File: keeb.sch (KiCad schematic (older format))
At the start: 134 parts, among them SW101 SW_Push, SW102 SW_Push, SW103 SW_Push, SW104 SW_Push, SW105 SW_Push, SW106 SW_Push, SW107 SW_Push, SW108 SW_Push, SW109 SW_Push, SW110 SW_Push, SW111 SW_Push, SW112 SW_Push, SW113 SW_Push, SW114 SW_Push, SW115 SW_Push, SW116 SW_Push, SW117 SW_Push, SW118 SW_Push, SW119 SW_Push, SW120 SW_Push, SW121 SW_Push, SW122 SW_Push, SW123 SW_Push, SW124 SW_Push, SW125 SW_Push, SW126 SW_Push, SW127 SW_Push, SW128 SW_Push, SW129 SW_Push, SW130 SW_Push, SW131 SW_Push, SW132 SW_Push, SW133 SW_Push, SW134 SW_Push, SW135 SW_Push, SW136 SW_Push, SW137 SW_Push, SW138 SW_Push, SW139 SW_Push, SW140 SW_Push, SW141 SW_Push, SW142 SW_Push, SW143 SW_Push, SW144 SW_Push, SW145 SW_Push, SW146 SW_Push, SW147 SW_Push, SW148 SW_Push, SW149 SW_Push, SW150 SW_Push, SW151 SW_Push, SW152 SW_Push, SW153 SW_Push, SW154 SW_Push, SW155 SW_Push, SW156 SW_Push, SW157 SW_Push, SW158 SW_Push, SW159 SW_Push, SW160 SW_Push, SW161 SW_Push, SW162 SW_Push, SW163 SW_Push, SW164 SW_Push, SW165 SW_Push, SW166 SW_Push

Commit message: schem compl, layout sw, mat  routing
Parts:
- added C101, C102, C103, C104, C105: 100n, Capacitor_SMD:C_0603_1608Metric_Pad1.08x0.95mm_HandSolder, symbol Device:C_Small
- added C106, C107: 20p, Capacitor_SMD:C_0603_1608Metric_Pad1.08x0.95mm_HandSolder, symbol Device:C_Small
- added C108: 1u, Capacitor_SMD:C_0603_1608Metric_Pad1.08x0.95mm_HandSolder, symbol Device:C_Small
- added F101: 500mA, Fuse:Fuse_1206_3216Metric_Pad1.42x1.75mm_HandSolder, symbol Device:Polyfuse_Small
- added J101: USB_C_Receptacle_USB2.0, Connector_USB:USB_C_Receptacle_Palconn_UTC16-G, symbol Connector:USB_C_Receptacle_USB2.0
- added R101, R102: 5K1, Resistor_SMD:R_0603_1608Metric_Pad0.98x0.95mm_HandSolder, symbol Device:R_Small
- added R103, R104: 22, Resistor_SMD:R_0603_1608Metric_Pad0.98x0.95mm_HandSolder, symbol Device:R_Small
- added R105, R106: 10k, Resistor_SMD:R_0603_1608Metric_Pad0.98x0.95mm_HandSolder, symbol Device:R_Small
- added SW167: SW_Push, Button_Switch_THT:SW_PUSH_6mm_H5mm, symbol Switch:SW_Push
- added U101: TPD2EUSB30, Package_TO_SOT_SMD:Texas_DRT-3, symbol Power_Protection:TPD2EUSB30
- added U102: ATmega32U4-AU, Package_QFP:TQFP-44_10x10mm_P0.8mm, symbol MCU_Microchip_ATmega:ATmega32U4-AU
- added Y101: 16MHZ/20PF, Crystal:Crystal_HC49-4H_Vertical, symbol Device:Crystal
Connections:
- net COL_0: now also U102.28 (PB4)
- net COL_1: now also U102.29 (PB5)
- net COL_10: now also U102.25 (PD4)
- net COL_11: now also U102.22 (PD5)
- net COL_12: now also U102.26 (PD6)
- net COL_13: now also U102.27 (PD7)
- net COL_2: now also U102.30 (PB6)
- net COL_3: now also U102.12 (PB7)
- net COL_4: now also U102.31 (PC6)
- net COL_5: now also U102.32 (PC7)
- net COL_6: now also U102.18 (PD0)
- net COL_7: now also U102.19 (PD1)
- net COL_8: now also U102.20 (PD2)
- net COL_9: now also U102.21 (PD3)
- net ROW_0: now also D113.1 (K), D114.1 (K), U102.41 (PF0)
- net ROW_1: now also U102.40 (PF1)
- net ROW_2: now also U102.39 (PF4)
- net ROW_3: now also U102.38 (PF5)
- net ROW_4: now also U102.37 (PF6)
- new net +5V: C101.1, C102.1, C103.1, C104.1, C105.1, F101.1, R105.2, U102.14 (VCC), U102.2 (UVCC), U102.24 (AVCC), U102.34 (VCC), U102.44 (AVCC), U102.7 (VBUS)
- new net CC1: J101.A5 (CC1), R101.1
- new net CC2: J101.B5 (CC2), R102.1
- new net D+: J101.A6 (D+), J101.B6 (D+), R103.2, U101.1 (D+)
- new net D-: J101.A7 (D-), J101.B7 (D-), R104.2, U101.2 (D-)
- new net GND: C101.2, C102.2, C103.2, C104.2, C105.2, C106.2, C107.2, C108.1, J101.A1 (GND), J101.A12 (GND), J101.B1 (GND), J101.B12 (GND), R101.2, R102.2, R106.1, SW167.2, U101.3 (GND), U102.15 (GND), U102.23 (GND), U102.35 (GND), U102.43 (GND), U102.5 (UGND)
- new net MISO: U102.11 (PB3)
- new net MOSI: U102.10 (PB2)
- new net SCLK: U102.9 (PB1)
- new net UCAP: C108.2, U102.6 (UCAP)
- new net USB+: R103.1, U102.4 (D+)
- new net USB-: R104.1, U102.3 (D-)
- new net VBUS: F101.2, J101.A4 (VBUS), J101.A9 (VBUS), J101.B4 (VBUS), J101.B9 (VBUS)
- new net XTAL1: C106.1, U102.17 (XTAL1), Y101.1
- new net XTAL2: C107.1, U102.16 (XTAL2), Y101.2
- new net ~HWB: R106.2, U102.33 (~HWB~/PE2)
- new net ~RESET: R105.1, SW167.1, U102.13 (~RESET)
- no-connect marks 0 -> 7
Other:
- moved on the sheet: D101, D102, D103, D104, D105, D106, D107, D108, D109, D110, D111, D112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

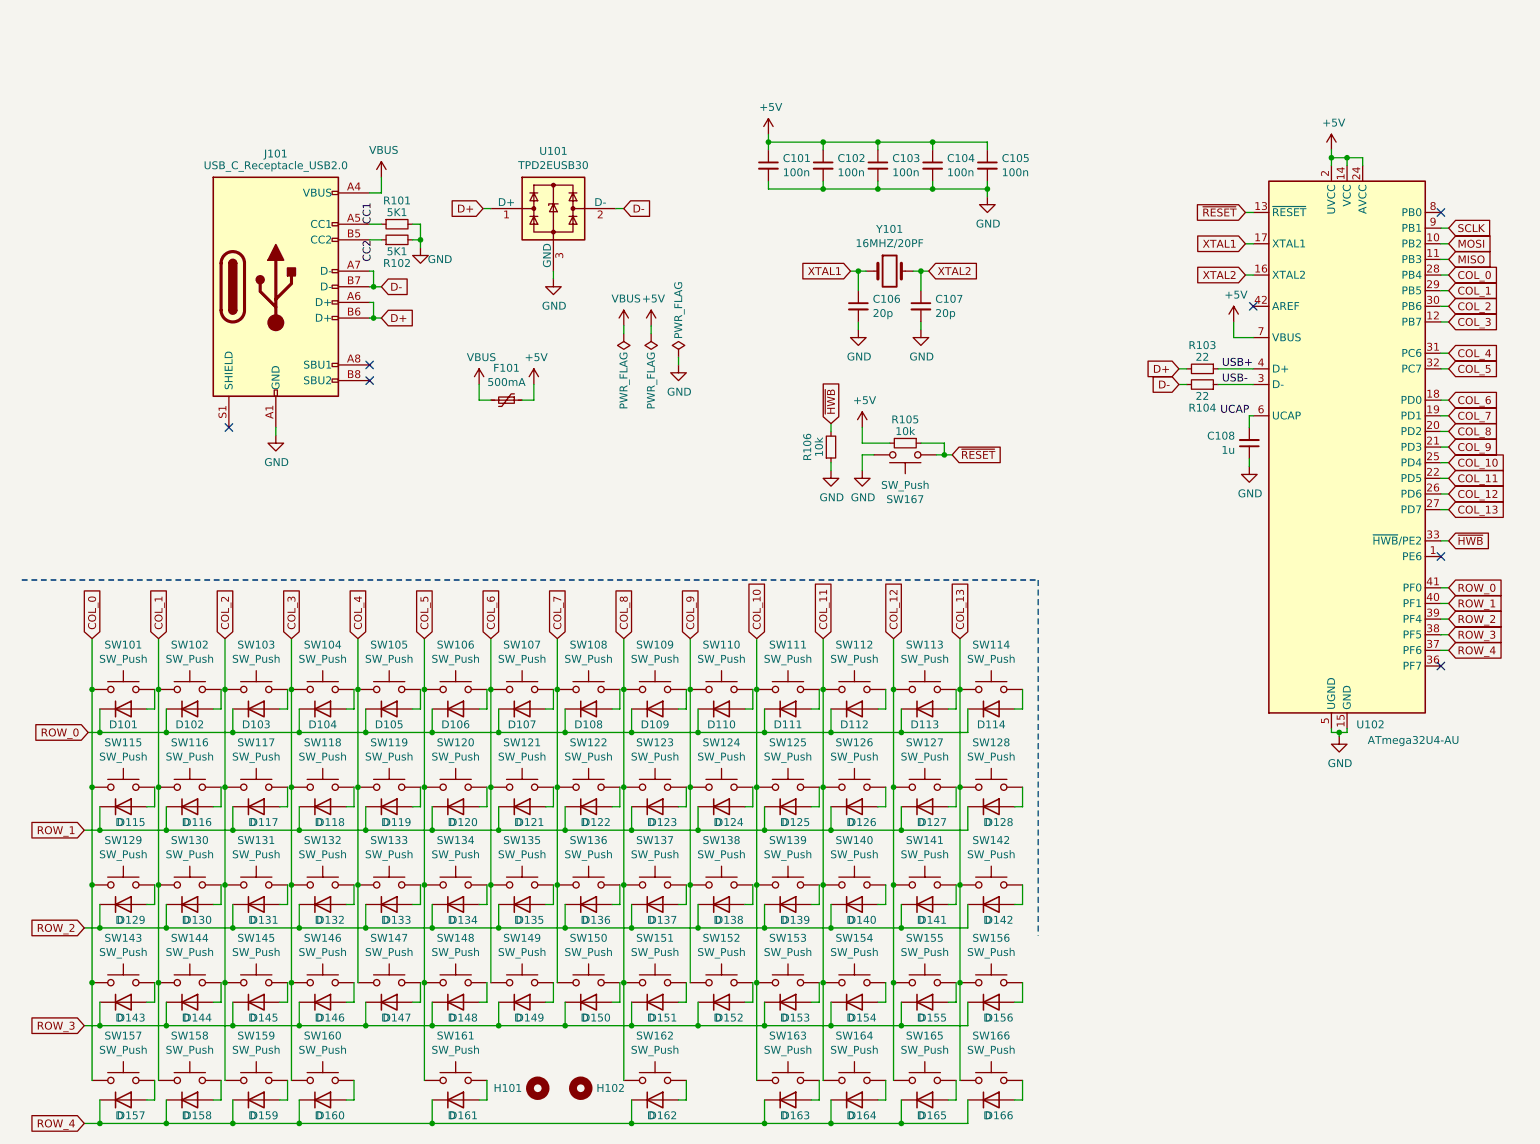
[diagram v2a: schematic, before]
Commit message: col, USB, and gnd layout
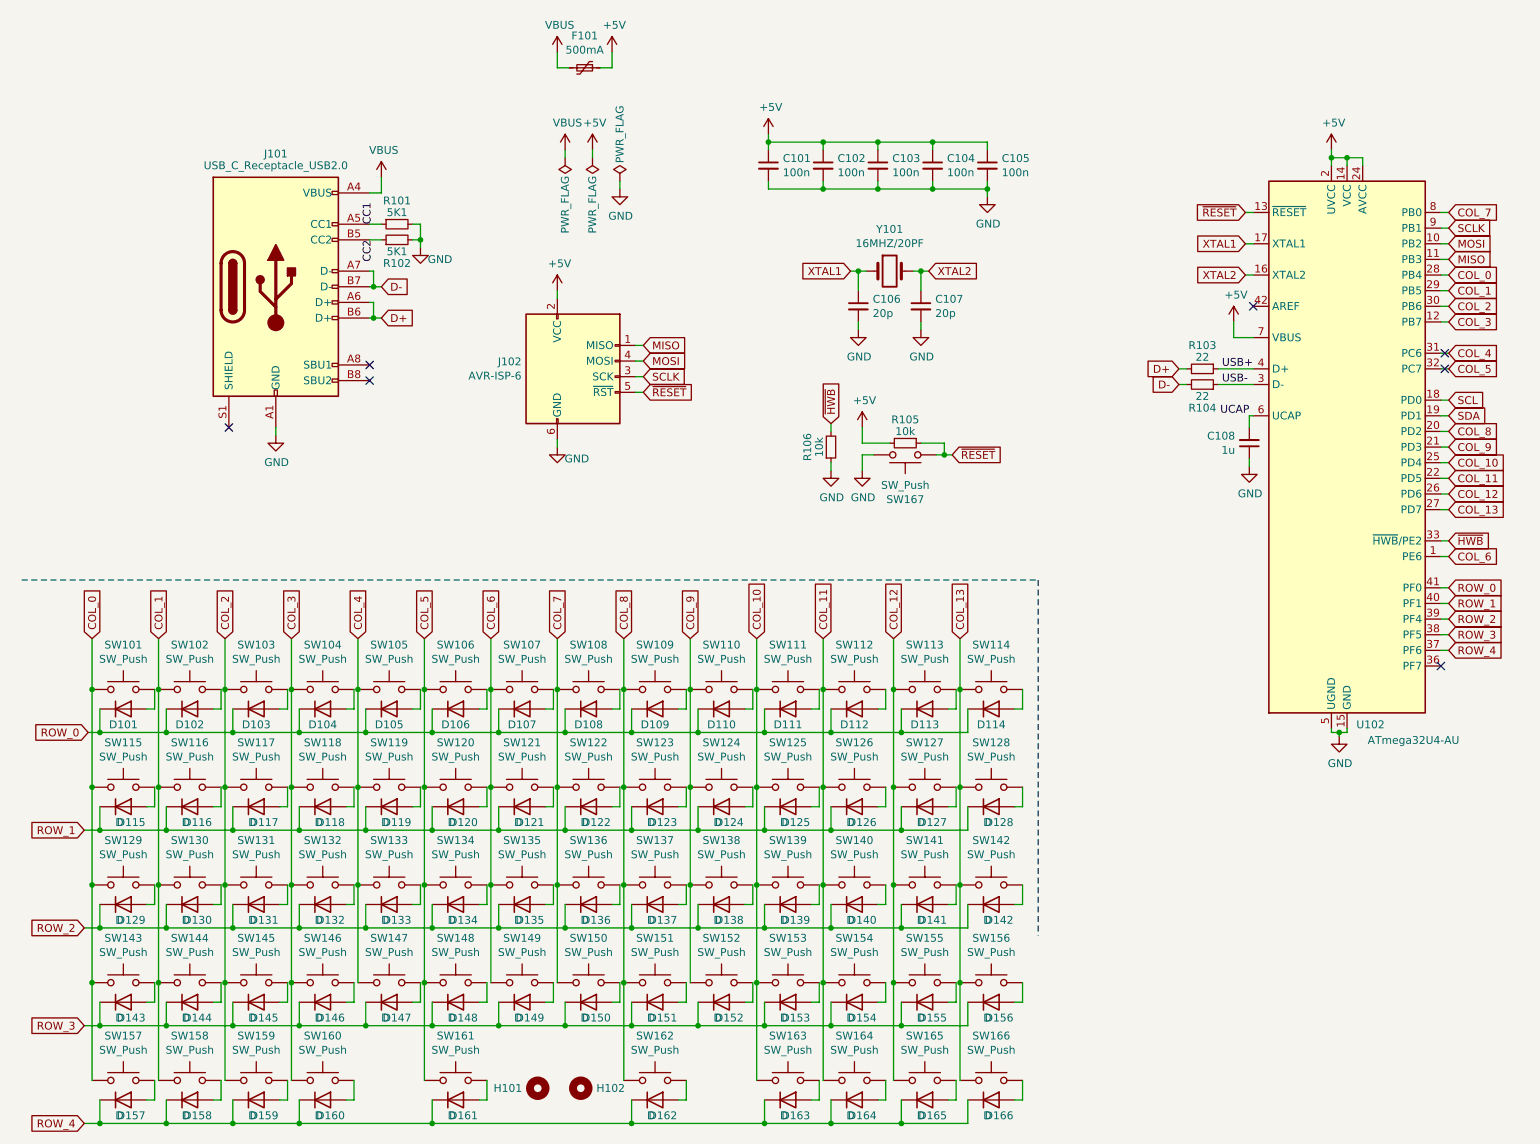
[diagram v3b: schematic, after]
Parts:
- removed U101: TPD2EUSB30, Package_TO_SOT_SMD:Texas_DRT-3, symbol Power_Protection:TPD2EUSB30
- added J102: AVR-ISP-6, Connector_PinHeader_2.54mm:PinHeader_2x03_P2.54mm_Vertical, symbol Connector:AVR-ISP-6
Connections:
- net +5V: now also J102.2 (VCC)
- net COL_6: now also U102.1 (PE6); no longer U102.18 (PD0)
- net COL_7: now also U102.8 (PB0); no longer U102.19 (PD1)
- net GND: now also J102.6 (GND)
- net MISO: now also J102.1 (MISO)
- net MOSI: now also J102.4 (MOSI)
- net SCLK: now also J102.3 (SCK)
- net ~RESET: now also J102.5 (~RST)
- new net SCL: U102.18 (PD0)
- new net SDA: U102.19 (PD1)
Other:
- moved on the sheet: F101
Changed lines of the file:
@@
 	6975 4250 6975 6525
-$Comp
-L MCU_Microchip_ATmega:ATmega32U4-AU U102
-U 1 1 61B6B293
-P 8950 3400
-F 0 "U102" H 9100 1625 50  0000 C CNN
-F 1 "ATmega32U4-AU" H 9375 1525 50  0000 C CNN
-F 2 "Package_QFP:TQFP-44_10x10mm_P0.8mm" H 8950 3400 50  0001 C CIN
-F 3 "http://ww1.microchip.com/downloads/en/DeviceDoc/Atmel-7766-8-bit-AVR-ATmega16U4-32U4_Datasheet.pdf" H 8950 3400 50  0001 C CNN
-	1    8950 3400
-	1    0    0    -1
-$EndComp
 $Comp
 L Connector:USB_C_Receptacle_USB2.0 J101
@@
 F 3 "https://www.usb.org/sites/default/files/documents/usb_type-c.zip" H 2250 2375 50  0001 C CNN
 	1    2100 2375
-	1    0    0    -1
-$EndComp
-$Comp
-L Power_Protection:TPD2EUSB30 U101
-U 1 1 61BD5C4D
-P 3875 1875
-F 0 "U101" H 3875 2242 50  0000 C CNN
-F 1 "TPD2EUSB30" H 3875 2151 50  0000 C CNN
-F 2 "Package_TO_SOT_SMD:Texas_DRT-3" H 3125 1575 50  0001 C CNN
-F 3 "http://www.ti.com/lit/ds/symlink/tpd2eusb30a.pdf" H 3875 1875 50  0001 C CNN
-	1    3875 1875
 	1    0    0    -1
 $EndComp
@@
 D+
 $Comp
-L power:GND #PWR0103
-U 1 1 61FAC895
-P 3875 2325
-F 0 "#PWR0103" H 3875 2075 50  0001 C CNN
-F 1 "GND" H 3880 2152 50  0000 C CNN
-F 2 "" H 3875 2325 50  0001 C CNN
-F 3 "" H 3875 2325 50  0001 C CNN
-	1    3875 2325
-	1    0    0    -1
-$EndComp
-Wire Wire Line
-	3875 2275 3875 2325
-Wire Wire Line
-	4275 1875 4325 1875
-Wire Wire Line
-	3475 1875 3425 1875
-Text GLabel 4325 1875 2    50   Input ~ 0
-D-
-Text GLabel 3425 1875 0    50   Input ~ 0
-D+
-$Comp
 L power:GND #PWR0104
 U 1 1 6202E960
@@
 L Device:Polyfuse_Small F101
 U 1 1 621B84EB
-P 3575 3100
-F 0 "F101" V 3370 3100 50  0000 C CNN
-F 1 "500mA" V 3461 3100 50  0000 C CNN
-F 2 "Fuse:Fuse_1206_3216Metric_Pad1.42x1.75mm_HandSolder" H 3625 2900 50  0001 L CNN
-F 3 "~" H 3575 3100 50  0001 C CNN
-	1    3575 3100
+P 4075 975
+F 0 "F101" V 3870 975 50  0000 C CNN
+F 1 "500mA" V 3961 975 50  0000 C CNN
+F 2 "Fuse:Fuse_1206_3216Metric_Pad1.42x1.75mm_HandSolder" H 4125 775 50  0001 L CNN
+F 3 "~" H 4075 975 50  0001 C CNN
+	1    4075 975
 	0    1    1    0
 $EndComp
@@
 L power:VBUS #PWR0105
 U 1 1 621BFE26
-P 3400 3000
-F 0 "#PWR0105" H 3400 2850 50  0001 C CNN
-F 1 "VBUS" H 3415 3173 50  0000 C CNN
-F 2 "" H 3400 3000 50  0001 C CNN
-F 3 "" H 3400 3000 50  0001 C CNN
-	1    3400 3000
+P 3900 875
+F 0 "#PWR0105" H 3900 725 50  0001 C CNN
+F 1 "VBUS" H 3915 1048 50  0000 C CNN
+F 2 "" H 3900 875 50  0001 C CNN
+F 3 "" H 3900 875 50  0001 C CNN
+	1    3900 875
 	1    0    0    -1
 $EndComp
@@
 L power:+5V #PWR0106
 U 1 1 621DD50C
-P 3750 3000
-F 0 "#PWR0106" H 3750 2850 50  0001 C CNN
-F 1 "+5V" H 3765 3173 50  0000 C CNN
-F 2 "" H 3750 3000 50  0001 C CNN
-F 3 "" H 3750 3000 50  0001 C CNN
-	1    3750 3000
-	1    0    0    -1
-$EndComp
-Wire Wire Line
-	3400 3000 3400 3100
-Wire Wire Line
-	3400 3100 3475 3100
-Wire Wire Line
-	3750 3000 3750 3100
-Wire Wire Line
-	3750 3100 3675 3100
+P 4250 875
+F 0 "#PWR0106" H 4250 725 50  0001 C CNN
+F 1 "+5V" H 4265 1048 50  0000 C CNN
+F 2 "" H 4250 875 50  0001 C CNN
+F 3 "" H 4250 875 50  0001 C CNN
+	1    4250 875
+	1    0    0    -1
+$EndComp
+Wire Wire Line
+	3900 875  3900 975
+Wire Wire Line
+	3900 975  3975 975
+Wire Wire Line
+	4250 875  4250 975
+Wire Wire Line
+	4250 975  4175 975
 $Comp
 L power:PWR_FLAG #FLG0101
 U 1 1 622C315C
-P 4325 2675
-F 0 "#FLG0101" H 4325 2750 50  0001 C CNN
-F 1 "PWR_FLAG" V 4325 2975 50  0000 C CNN
-F 2 "" H 4325 2675 50  0001 C CNN
-F 3 "~" H 4325 2675 50  0001 C CNN
-	1    4325 2675
+P 3950 1550
+F 0 "#FLG0101" H 3950 1625 50  0001 C CNN
+F 1 "PWR_FLAG" V 3950 1850 50  0000 C CNN
+F 2 "" H 3950 1550 50  0001 C CNN
+F 3 "~" H 3950 1550 50  0001 C CNN
+	1    3950 1550
 	-1   0    0    1
 $EndComp
@@
 L power:PWR_FLAG #FLG0102
 U 1 1 622C3D5C
-P 4500 2675
-F 0 "#FLG0102" H 4500 2750 50  0001 C CNN
-F 1 "PWR_FLAG" V 4500 2975 50  0000 C CNN
-F 2 "" H 4500 2675 50  0001 C CNN
-F 3 "~" H 4500 2675 50  0001 C CNN
-	1    4500 2675
+P 4125 1550
+F 0 "#FLG0102" H 4125 1625 50  0001 C CNN
+F 1 "PWR_FLAG" V 4125 1850 50  0000 C CNN
+F 2 "" H 4125 1550 50  0001 C CNN
+F 3 "~" H 4125 1550 50  0001 C CNN
+	1    4125 1550
 	-1   0    0    1
 $EndComp
@@
 L power:VBUS #PWR0107
 U 1 1 622E193B
-P 4325 2625
-F 0 "#PWR0107" H 4325 2475 50  0001 C CNN
-F 1 "VBUS" H 4340 2798 50  0000 C CNN
-F 2 "" H 4325 2625 50  0001 C CNN
-F 3 "" H 4325 2625 50  0001 C CNN
-	1    4325 2625
+P 3950 1500
+F 0 "#PWR0107" H 3950 1350 50  0001 C CNN
+F 1 "VBUS" H 3965 1673 50  0000 C CNN
+F 2 "" H 3950 1500 50  0001 C CNN
+F 3 "" H 3950 1500 50  0001 C CNN
+	1    3950 1500
 	1    0    0    -1
 $EndComp
@@
 L power:+5V #PWR0108
 U 1 1 622FFCBC
-P 4500 2625
-F 0 "#PWR0108" H 4500 2475 50  0001 C CNN
-F 1 "+5V" H 4515 2798 50  0000 C CNN
-F 2 "" H 4500 2625 50  0001 C CNN
-F 3 "" H 4500 2625 50  0001 C CNN
-	1    4500 2625
+P 4125 1500
+F 0 "#PWR0108" H 4125 1350 50  0001 C CNN
+F 1 "+5V" H 4140 1673 50  0000 C CNN
+F 2 "" H 4125 1500 50  0001 C CNN
+F 3 "" H 4125 1500 50  0001 C CNN
+	1    4125 1500
 	1    0    0    -1
 $EndComp
@@
 L power:GND #PWR0109
 U 1 1 62358EE0
-P 4675 2875
-F 0 "#PWR0109" H 4675 2625 50  0001 C CNN
-F 1 "GND" H 4680 2702 50  0000 C CNN
-F 2 "" H 4675 2875 50  0001 C CNN
-F 3 "" H 4675 2875 50  0001 C CNN
-	1    4675 2875
-	1    0    0    -1
-$EndComp
-Wire Wire Line
-	4675 2825 4675 2875
-Wire Wire Line
-	4325 2675 4325 2625
-Wire Wire Line
-	4500 2675 4500 2625
+P 4300 1750
+F 0 "#PWR0109" H 4300 1500 50  0001 C CNN
+F 1 "GND" H 4305 1577 50  0000 C CNN
+F 2 "" H 4300 1750 50  0001 C CNN
+F 3 "" H 4300 1750 50  0001 C CNN
+	1    4300 1750
+	1    0    0    -1
+$EndComp
+Wire Wire Line
+	4300 1700 4300 1750
+Wire Wire Line
+	3950 1550 3950 1500
+Wire Wire Line
+	4125 1550 4125 1500
 $Comp
 L power:PWR_FLAG #FLG0103
 U 1 1 6231ED4A
-P 4675 2825
-F 0 "#FLG0103" H 4675 2900 50  0001 C CNN
-F 1 "PWR_FLAG" V 4675 3125 50  0000 C CNN
-F 2 "" H 4675 2825 50  0001 C CNN
-F 3 "~" H 4675 2825 50  0001 C CNN
-	1    4675 2825
+P 4300 1700
+F 0 "#FLG0103" H 4300 1775 50  0001 C CNN
+F 1 "PWR_FLAG" V 4300 2000 50  0000 C CNN
+F 2 "" H 4300 1700 50  0001 C CNN
+F 3 "~" H 4300 1700 50  0001 C CNN
+	1    4300 1700
 	1    0    0    -1
 $EndComp
@@
 Wire Wire Line
 	8300 1900 8350 1900
-Text GLabel 8300 1900 0    50   Input ~ 0
-~RESET
 Text GLabel 8300 2100 0    50   Input ~ 0
 XTAL1
@@
 	1    0    0    -1
 $EndComp
-Text GLabel 6425 3450 2    50   Input ~ 0
-~RESET
 Wire Wire Line
 	6325 3450 6375 3450
@@
 Text GLabel 9600 2900 2    50   Input ~ 0
 COL_5
-Text GLabel 9600 3100 2    50   Input ~ 0
+Text GLabel 9600 4100 2    50   Input ~ 0
 COL_6
-Text GLabel 9600 3200 2    50   Input ~ 0
+Text GLabel 9600 1900 2    50   Input ~ 0
 COL_7
 Text GLabel 9600 3300 2    50   Input ~ 0
@@
 	9550 2900 9600 2900
 Wire Wire Line
-	9600 3100 9550 3100
-Wire Wire Line
-	9550 3200 9600 3200
+	9600 4100 9550 4100
+Wire Wire Line
+	9550 1900 9600 1900
 Wire Wire Line
 	9600 3300 9550 3300
@@
 Wire Wire Line
 	9550 3800 9600 3800
-NoConn ~ 9550 1900
 Wire Wire Line
 	5650 5225 6100 5225
@@
 Text Label 8150 3000 0    50   ~ 0
 USB-
-NoConn ~ 9550 4100
 Text Label 8325 3200 2    50   ~ 0
 UCAP
@@
 Text Label 2725 2075 3    50   ~ 0
 CC2
+$Comp
+L Connector:AVR-ISP-6 J102
+U 1 1 61C04FF9
+P 4000 2950
+F 0 "J102" H 3671 3046 50  0000 R CNN
+F 1 "AVR-ISP-6" H 3671 2955 50  0000 R CNN
+F 2 "Connector_PinHeader_2.54mm:PinHeader_2x03_P2.54mm_Vertical" V 3750 3000 50  0001 C CNN
+F 3 " ~" H 2725 2400 50  0001 C CNN
+	1    4000 2950
+	1    0    0    -1
+$EndComp
+$Comp
+L power:+5V #PWR0103
+U 1 1 61C97E73
+P 3900 2400
+F 0 "#PWR0103" H 3900 2250 50  0001 C CNN
+F 1 "+5V" H 3915 2573 50  0000 C CNN
+F 2 "" H 3900 2400 50  0001 C CNN
+F 3 "" H 3900 2400 50  0001 C CNN
+	1    3900 2400
+	1    0    0    -1
+$EndComp
+Wire Wire Line
+	3900 2400 3900 2450
+$Comp
+L power:GND #PWR0121
+U 1 1 61D40582
+P 3900 3400
+F 0 "#PWR0121" H 3900 3150 50  0001 C CNN
+F 1 "GND" H 4025 3325 50  0000 C CNN
+F 2 "" H 3900 3400 50  0001 C CNN
+F 3 "" H 3900 3400 50  0001 C CNN
+	1    3900 3400
+	1    0    0    -1
+$EndComp
+Wire Wire Line
+	3900 3350 3900 3400
+Text GLabel 4450 2950 2    50   Input ~ 0
+SCLK
+Text GLabel 4450 2850 2    50   Input ~ 0
+MOSI
+Text GLabel 4450 2750 2    50   Input ~ 0
+MISO
+Wire Wire Line
+	4400 2950 4450 2950
+Wire Wire Line
+	4450 2850 4400 2850
+Wire Wire Line
+	4400 2750 4450 2750
+Text GLabel 8300 1900 0    50   Input ~ 0
+~RESET
+Text GLabel 6425 3450 2    50   Input ~ 0
+~RESET
+Text GLabel 4450 3050 2    50   Input ~ 0
+~RESET
+Wire Wire Line
+	4400 3050 4450 3050
+$Comp
+L MCU_Microchip_ATmega:ATmega32U4-AU U102
+U 1 1 61B6B293
+P 8950 3400
+F 0 "U102" H 9100 1625 50  0000 C CNN
+F 1 "ATmega32U4-AU" H 9375 1525 50  0000 C CNN
+F 2 "Package_QFP:TQFP-44_10x10mm_P0.8mm" H 8950 3400 50  0001 C CIN
+F 3 "http://ww1.microchip.com/downloads/en/DeviceDoc/Atmel-7766-8-bit-AVR-ATmega16U4-32U4_Datasheet.pdf" H 8950 3400 50  0001 C CNN
+	1    8950 3400
+	1    0    0    -1
+$EndComp
+Wire Wire Line
+	9550 3100 9600 3100
+Wire Wire Line
+	9550 3200 9600 3200
+Text GLabel 9600 3100 2    50   Input ~ 0
+SCL
+Text GLabel 9600 3200 2    50   Input ~ 0
+SDA
+NoConn ~ 9575 2800
+NoConn ~ 9575 2900
 $EndSCHEMATC

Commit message: models3D
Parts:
- removed Y101: 16MHZ/20PF, Crystal:Crystal_HC49-4H_Vertical, symbol Device:Crystal
- added J1: AudioJack3, Connector_Audio:Jack_3.5mm_CUI_SJ-3523-SMT_Horizontal, symbol Connector:AudioJack3
- added Y1: 16Mhz, Crystal:Crystal_SMD_2016-4Pin_2.0x1.6mm, symbol Device:Crystal_GND24_Small
- C106, C107: value 20p -> 22p
- U102: symbol MCU_Microchip_ATmega:ATmega32U4-AU -> keeb-rescue:ATmega32U4-AU-MCU_Microchip_ATmega
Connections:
- net GND: now also Y1.2, Y1.4
- net SCL: now also J1.R
- net SDA: now also J1.S
- net XTAL1: now also Y1.1
- net XTAL2: now also Y1.3
- no-connect marks 7 -> 6
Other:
- moved on the sheet: C101, C102, C103, C104, C105, C106, C107, C108, F101, J101, J102, R101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
